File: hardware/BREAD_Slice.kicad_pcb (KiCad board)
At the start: 2 copper layers, 72.6 x 100 mm, 16 parts, among them J1 Conn_01x10_Female, J2 I2C_01x04

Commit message: Initial commit
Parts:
- removed C3, C4: 22uF, Capacitor_SMD:C_1206_3216Metric
- removed D1: WS2812B_5050, SparkFun-LED:WS2812-5050-4PIN
- removed HS1: Heatsink_Pad, SparkFun-Fuse:Thermal Pad
- removed L1: 4.7uH, Inductor_SMD:L_1210_3225Metric
- added J3: Screw_Terminal_01x02, TerminalBlock_TE-Connectivity:TerminalBlock_TE_282834-2_1x02_P2.54mm_Horizontal, F.Cu at (187.8, 83.5)
- added J4: Screw_Terminal_01x02, TerminalBlock_TE-Connectivity:TerminalBlock_TE_282834-2_1x02_P2.54mm_Horizontal, F.Cu at (188.0, 106.7)
- added J5: Screw_Terminal_01x02, TerminalBlock_TE-Connectivity:TerminalBlock_TE_282834-2_1x02_P2.54mm_Horizontal, F.Cu at (188.1, 60.3)
- added U2: ACS723xMATR-10AB, Package_SO:SOIC-16W_7.5x10.3mm_P1.27mm, B.Cu at (175.8, 82.1)
- added U3: ACS723xMATR-10AB, Package_SO:SOIC-16W_7.5x10.3mm_P1.27mm, B.Cu at (175.6, 105.1)
- added U4: ACS723xMATR-10AB, Package_SO:SOIC-16W_7.5x10.3mm_P1.27mm, B.Cu at (175.8, 58.8)
- C1: value 22uF -> 10uF_t; footprint Capacitor_SMD:C_1206_3216Metric -> OCI_UPL_FOOTPRINTS:C_2312
- C2: value 100nF -> 10uF_t; footprint Capacitor_SMD:C_1206_3216Metric -> OCI_UPL_FOOTPRINTS:C_2312
- H1, H4: footprint MountingHole:MountingHole_5mm -> MountingHole:MountingHole_3.2mm_M3_DIN965_Pad
- H2: renamed from H3; footprint MountingHole:MountingHole_5mm -> MountingHole:MountingHole_3.2mm_M3_DIN965_Pad
- H3: renamed from H2; footprint MountingHole:MountingHole_5mm -> MountingHole:MountingHole_3.2mm_M3_DIN965_Pad
- J2: value I2C_01x04 -> Screw_Terminal_01x02; footprint Connector_JST:JST_SH_SM04B-SRSS-TB_1x04-1MP_P1.00mm_Horizontal -> TerminalBlock_TE-Connectivity:TerminalBlock_TE_282834-2_1x02_P2.54mm_Horizontal; moved to F.Cu
- U1: value ~ -> ACS723xMATR-10AB; footprint Package_TO_SOT_SMD:TSOT-23-6 -> Package_SO:SOIC-16W_7.5x10.3mm_P1.27mm
- moved Logo1 76.2 mm to (168.3, 136.0), turned to 0 degrees
- moved U1 47.5 mm to (176.2, 125.4), turned to 180 degrees
- moved J2 38.7 mm to (187.8, 127.0), turned to 90 degrees
- moved C1 37.9 mm to (150.3, 88.4), turned to 90 degrees
- moved C2 27.7 mm to (154.2, 110.8), turned to -90 degrees
- moved A1 7.59 mm to (135.0, 100.0)
- moved J1 3.43 mm to (129.6, 78.8)
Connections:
- A1 pad 1: unconnected-(A1-D1/TX-Pad1) -> Net-(A1-Pad1)
- A1 pad 10: unconnected-(A1-D7-Pad10) -> Net-(A1-Pad10)
- A1 pad 11: unconnected-(A1-D8-Pad11) -> Net-(A1-Pad11)
- A1 pad 12: unconnected-(A1-D9-Pad12) -> Net-(A1-Pad12)
- A1 pad 13: unconnected-(A1-D10-Pad13) -> Net-(A1-Pad13)
- A1 pad 14: unconnected-(A1-D11-Pad14) -> Net-(A1-Pad14)
- A1 pad 15: unconnected-(A1-D12-Pad15) -> Net-(A1-Pad15)
- A1 pad 16: unconnected-(A1-D13-Pad16) -> Net-(A1-Pad16)
- A1 pad 17: unconnected-(A1-3V3-Pad17) -> Net-(A1-Pad17)
- A1 pad 18: unconnected-(A1-AREF-Pad18) -> Net-(A1-Pad18)
- A1 pad 19: unconnected-(A1-A0-Pad19) -> /CURR1
- A1 pad 2: unconnected-(A1-D0/RX-Pad2) -> Net-(A1-Pad2)
- A1 pad 20: unconnected-(A1-A1-Pad20) -> /CURR2
- A1 pad 21: unconnected-(A1-A2-Pad21) -> /CURR3
- A1 pad 22: unconnected-(A1-A3-Pad22) -> /CURR4
- A1 pad 25: unconnected-(A1-A6-Pad25) -> Net-(A1-Pad25)
- A1 pad 26: unconnected-(A1-A7-Pad26) -> Net-(A1-Pad26)
- A1 pad 28: unconnected-(A1-~{RESET}-Pad28) -> Net-(A1-Pad28)
- A1 pad 3: unconnected-(A1-~{RESET}-Pad3) -> Net-(A1-Pad3)
- A1 pad 30: unconnected-(A1-VIN-Pad30) -> +12V
- A1 pad 8: /LED -> Net-(A1-Pad8)
- A1 pad 9: unconnected-(A1-D6-Pad9) -> Net-(A1-Pad9)
- C1 pad 1: GND -> +12V
- C1 pad 2: +12V -> GND
- C2 pad 1: Net-(U1-SW) -> +5V
- C2 pad 2: Net-(U1-BST) -> GND
- J2 pad 1: GND -> Net-(J2-Pad1)
- J2 pad 2: +5V -> Net-(J2-Pad2)
- U1 pad 1: +5V -> Net-(J2-Pad2)
- U1 pad 2: +12V -> Net-(J2-Pad2)
- U1 pad 3: +12V -> Net-(J2-Pad2)
- U1 pad 4: GND -> Net-(J2-Pad2)
- U1 pad 5: Net-(U1-SW) -> Net-(J2-Pad1)
- U1 pad 6: Net-(U1-BST) -> Net-(J2-Pad1)
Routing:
- net +5V: track 108.9 -> 188.6 mm, vias 1 -> 0
- net /CURR4: track 0.00 -> 77.8 mm
- net /CURR3: track 0.00 -> 56.6 mm
- net /LED: track 51.5 -> 0.00 mm
- net /CURR2: track 0.00 -> 36.1 mm
- net /I2C_CLK: track 78.5 -> 46.0 mm, vias 2 -> 0
- net /I2C_DAT: track 76.6 -> 46.4 mm, vias 2 -> 0
- net /CURR1: track 0.00 -> 22.1 mm
- net +12V: track 46.8 -> 58.5 mm
- net GND: track 19.6 -> 30.9 mm, vias 14 -> 0
- net /E_STOP: track 30.1 -> 22.3 mm
- net /INT: track 28.8 -> 22.6 mm
- net /SYNC: track 27.9 -> 22.2 mm
- net Net-(U1-SW): track 5.22 -> 0.00 mm
- net Net-(U1-BST): track 2.64 -> 0.00 mm
- added copper zone on B.Cu, net Net-(J2-Pad1)
- added copper zone on B.Cu, net Net-(J2-Pad2)
- added copper zone on B.Cu, net Net-(J3-Pad1)
- added copper zone on B.Cu, net Net-(J3-Pad2)
- added copper zone on B.Cu, net Net-(J4-Pad1)
- added copper zone on B.Cu, net Net-(J4-Pad2)
- added copper zone on B.Cu, net Net-(J5-Pad1)
- added copper zone on B.Cu, net Net-(J5-Pad2)
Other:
- board size 72.6 x 100 mm -> 70 x 100 mm
- board text added: "10A Current Slice SLC_CR10 R0 2021"
- board text removed: "12V"
- board text removed: "12V->5V Reg"
- board text removed: "5V I2C Connector"
- board text removed: "ARDUINO NANO"
- board text removed: "BREAD Slice Template SLC_TEMP <version> <year>"
- board text removed: "ESTOP"
- board text removed: "GND"
- board text removed: "INT"
- board text removed: "LED"
- board text removed: "SCL"
- board text removed: "SDA"
- board text removed: "SYNC"

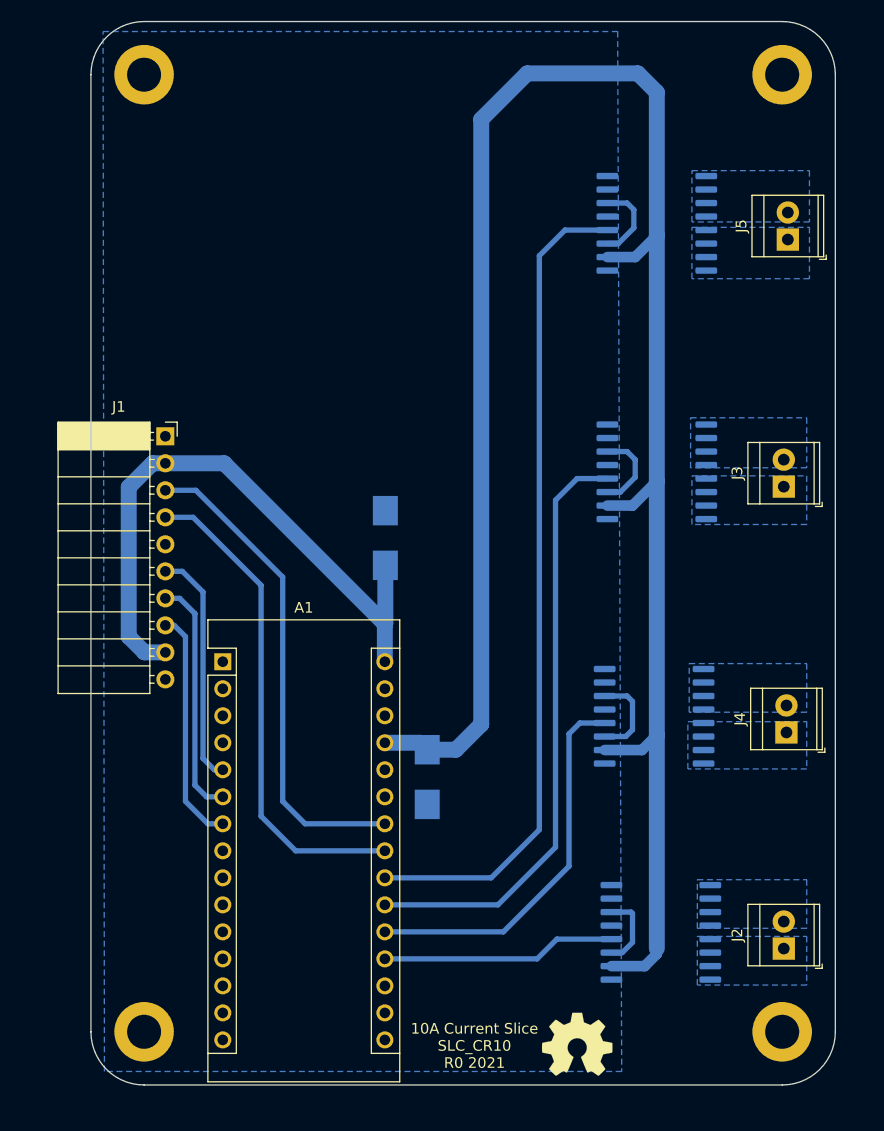
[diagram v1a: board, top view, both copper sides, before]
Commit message: updated to new BREAD format
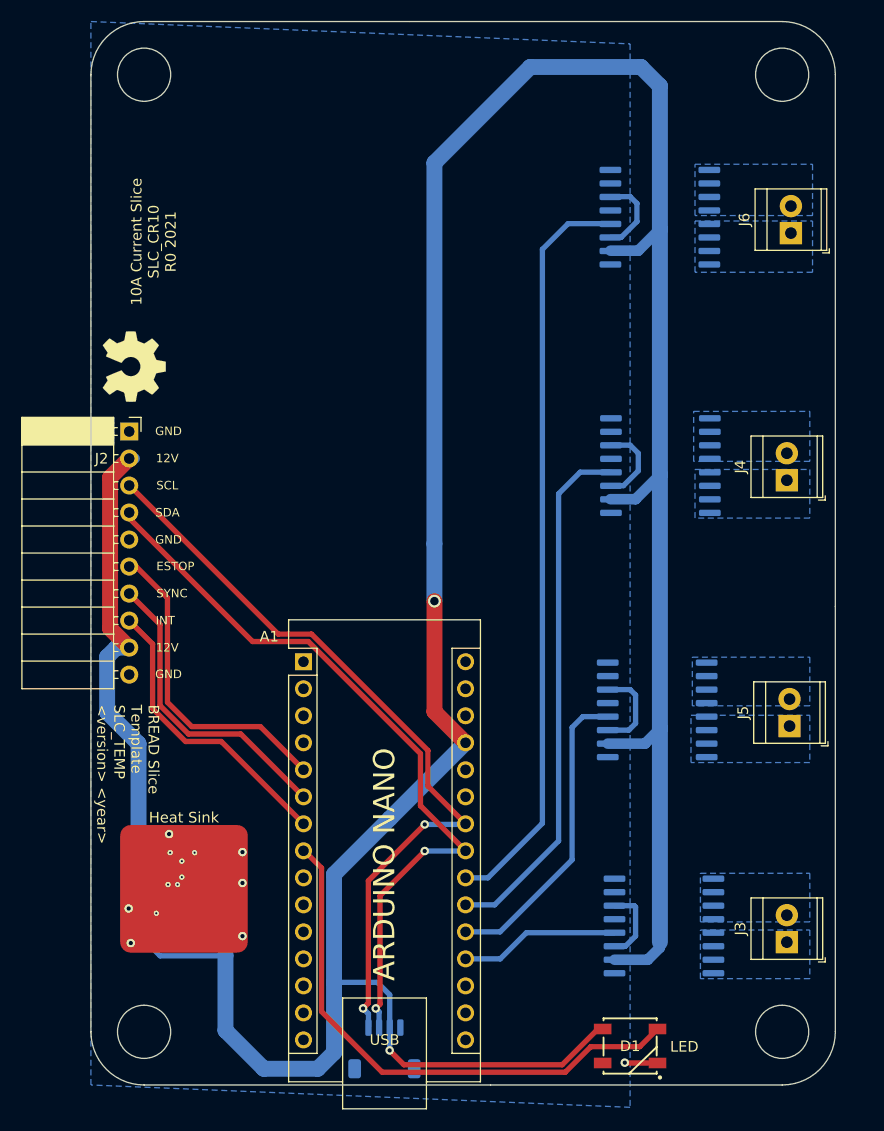
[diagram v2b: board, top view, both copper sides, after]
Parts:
- removed the J2 at (187.8, 127.0)
- added C3: 22uF, Capacitor_SMD:C_1206_3216Metric, B.Cu at (133.8, 119.5)
- added C4: 22uF, Capacitor_SMD:C_1206_3216Metric, B.Cu at (133.8, 116.5)
- added D1: WS2812B_5050, SparkFun-LED:WS2812-5050-4PIN, F.Cu at (173.3, 136.1)
- added HS1: Heatsink_Pad, KML-Custom:Thermal Pad, F.Cu at (131.3, 121.4)
- added J1: I2C_01x04, Connector_JST:JST_SH_SM04B-SRSS-TB_1x04-1MP_P1.00mm_Horizontal, B.Cu at (150.2, 136.4)
- added J6: Screw_Terminal_01x02, TerminalBlock_TE-Connectivity:TerminalBlock_TE_282834-2_1x02_P2.54mm_Horizontal, F.Cu at (188.4, 59.7)
- added L1: 4.7uH, Inductor_SMD:L_1210_3225Metric, B.Cu at (133.8, 122.8)
- added U5: ACS723xMATR-10AB, Package_SO:SOIC-16W_7.5x10.3mm_P1.27mm, B.Cu at (176.1, 58.2)
- C1: value 10uF_t -> 22uF; footprint OCI_UPL_FOOTPRINTS:C_2312 -> Capacitor_SMD:C_1206_3216Metric
- C2: value 10uF_t -> 100nF; footprint OCI_UPL_FOOTPRINTS:C_2312 -> Capacitor_SMD:C_1206_3216Metric
- H1, H4: footprint MountingHole:MountingHole_3.2mm_M3_DIN965_Pad -> MountingHole:MountingHole_5mm
- H2: renamed from H3; footprint MountingHole:MountingHole_3.2mm_M3_DIN965_Pad -> MountingHole:MountingHole_5mm
- H3: renamed from H2; footprint MountingHole:MountingHole_3.2mm_M3_DIN965_Pad -> MountingHole:MountingHole_5mm
- U1: value ACS723xMATR-10AB -> ~; footprint Package_SO:SOIC-16W_7.5x10.3mm_P1.27mm -> Package_TO_SOT_SMD:TSOT-23-6
- moved Logo1 76.2 mm to (126.7, 72.2), turned to -90 degrees
- moved U1 47.5 mm to (128.8, 122.8), turned to 0 degrees
- moved J5 45.8 mm to (188.3, 106.1)
- moved U4 45.8 mm to (175.8, 104.5)
- moved J3 42.8 mm to (188.0, 126.4)
- moved U2 42.7 mm to (176.5, 124.8)
- moved C1 37.9 mm to (128.6, 119.5), turned to 180 degrees
- moved C2 27.7 mm to (131.2, 126.3), turned to 180 degrees
- moved J4 23.7 mm to (188.0, 82.9)
- moved U3 23.6 mm to (176.2, 81.6)
- moved A1 7.59 mm to (142.6, 100.0)
- moved J2 3.43 mm to (126.2, 78.3)
- renumbered J1 to J2
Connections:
- A1 pad 1: Net-(A1-Pad1) -> unconnected-(A1-D1/TX-Pad1)
- A1 pad 10: Net-(A1-Pad10) -> unconnected-(A1-D7-Pad10)
- A1 pad 11: Net-(A1-Pad11) -> unconnected-(A1-D8-Pad11)
- A1 pad 12: Net-(A1-Pad12) -> unconnected-(A1-D9-Pad12)
- A1 pad 13: Net-(A1-Pad13) -> unconnected-(A1-D10-Pad13)
- A1 pad 14: Net-(A1-Pad14) -> unconnected-(A1-D11-Pad14)
- A1 pad 15: Net-(A1-Pad15) -> unconnected-(A1-D12-Pad15)
- A1 pad 16: Net-(A1-Pad16) -> unconnected-(A1-D13-Pad16)
- A1 pad 17: Net-(A1-Pad17) -> unconnected-(A1-3V3-Pad17)
- A1 pad 18: Net-(A1-Pad18) -> unconnected-(A1-AREF-Pad18)
- A1 pad 2: Net-(A1-Pad2) -> unconnected-(A1-D0/RX-Pad2)
- A1 pad 25: Net-(A1-Pad25) -> unconnected-(A1-A6-Pad25)
- A1 pad 26: Net-(A1-Pad26) -> unconnected-(A1-A7-Pad26)
- A1 pad 28: Net-(A1-Pad28) -> unconnected-(A1-~{RESET}-Pad28)
- A1 pad 3: Net-(A1-Pad3) -> unconnected-(A1-~{RESET}-Pad3)
- A1 pad 30: +12V -> unconnected-(A1-VIN-Pad30)
- A1 pad 8: Net-(A1-Pad8) -> /LED
- A1 pad 9: Net-(A1-Pad9) -> unconnected-(A1-D6-Pad9)
- C1 pad 1: +12V -> GND
- C1 pad 2: GND -> +12V
- C2 pad 1: +5V -> Net-(U1-SW)
- C2 pad 2: GND -> Net-(U1-BST)
- U1 pad 1: Net-(J2-Pad2) -> +5V
- U1 pad 2: Net-(J2-Pad2) -> +12V
- U1 pad 3: Net-(J2-Pad2) -> +12V
- U1 pad 4: Net-(J2-Pad2) -> GND
- U1 pad 5: Net-(J2-Pad1) -> Net-(U1-SW)
- U1 pad 6: Net-(J2-Pad1) -> Net-(U1-BST)
- U2 pad 12: /CURR3 -> /CURR1
- U2 pad 16: Net-(U2-Pad16) -> unconnected-(U2-NC-Pad16)
- U2 pad 9: Net-(U2-Pad9) -> unconnected-(U2-NC-Pad9)
- U3 pad 12: /CURR2 -> /CURR3
- U3 pad 16: Net-(U3-Pad16) -> unconnected-(U3-NC-Pad16)
- U3 pad 9: Net-(U3-Pad9) -> unconnected-(U3-NC-Pad9)
- U4 pad 12: /CURR4 -> /CURR2
- U4 pad 16: Net-(U4-Pad16) -> unconnected-(U4-NC-Pad16)
- U4 pad 9: Net-(U4-Pad9) -> unconnected-(U4-NC-Pad9)
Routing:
- net +5V: track 188.6 -> 292.7 mm, vias 0 -> 2
- net /LED: track 0.00 -> 51.5 mm
- net /I2C_CLK: track 46.0 -> 72.3 mm, vias 0 -> 2
- net /I2C_DAT: track 46.4 -> 70.5 mm, vias 0 -> 2
- net GND: track 30.9 -> 50.5 mm, vias 0 -> 14
- net +12V: track 58.5 -> 46.8 mm
- net /E_STOP: track 22.3 -> 30.1 mm
- net /CURR4: track 77.8 -> 70.7 mm
- net /CURR1: track 22.1 -> 15.0 mm
- net /CURR3: track 56.6 -> 49.6 mm
- net /CURR2: track 36.1 -> 29.0 mm
- net /INT: track 22.6 -> 28.8 mm
- net /SYNC: track 22.2 -> 27.9 mm
- net Net-(U1-SW): track 0.00 -> 5.22 mm
- net Net-(U1-BST): track 0.00 -> 2.64 mm
- added copper zone on B.Cu, net Net-(J6-Pin_1)
- added copper zone on B.Cu, net Net-(J6-Pin_2)
- removed copper zone on B.Cu, net Net-(J2-Pad1)
- removed copper zone on B.Cu, net Net-(J2-Pad2)
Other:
- outline, holes or cut-outs redrawn
- board text added: "12V"
- board text added: "12V->5V Reg"
- board text added: "5V I2C Connector"
- board text added: "ARDUINO NANO"
- board text added: "BREAD Slice Template SLC_TEMP <version> <year>"
- board text added: "ESTOP"
- board text added: "GND"
- board text added: "INT"
- board text added: "LED"
- board text added: "SCL"
- board text added: "SDA"
- board text added: "SYNC"

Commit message: updated for CRxx forking
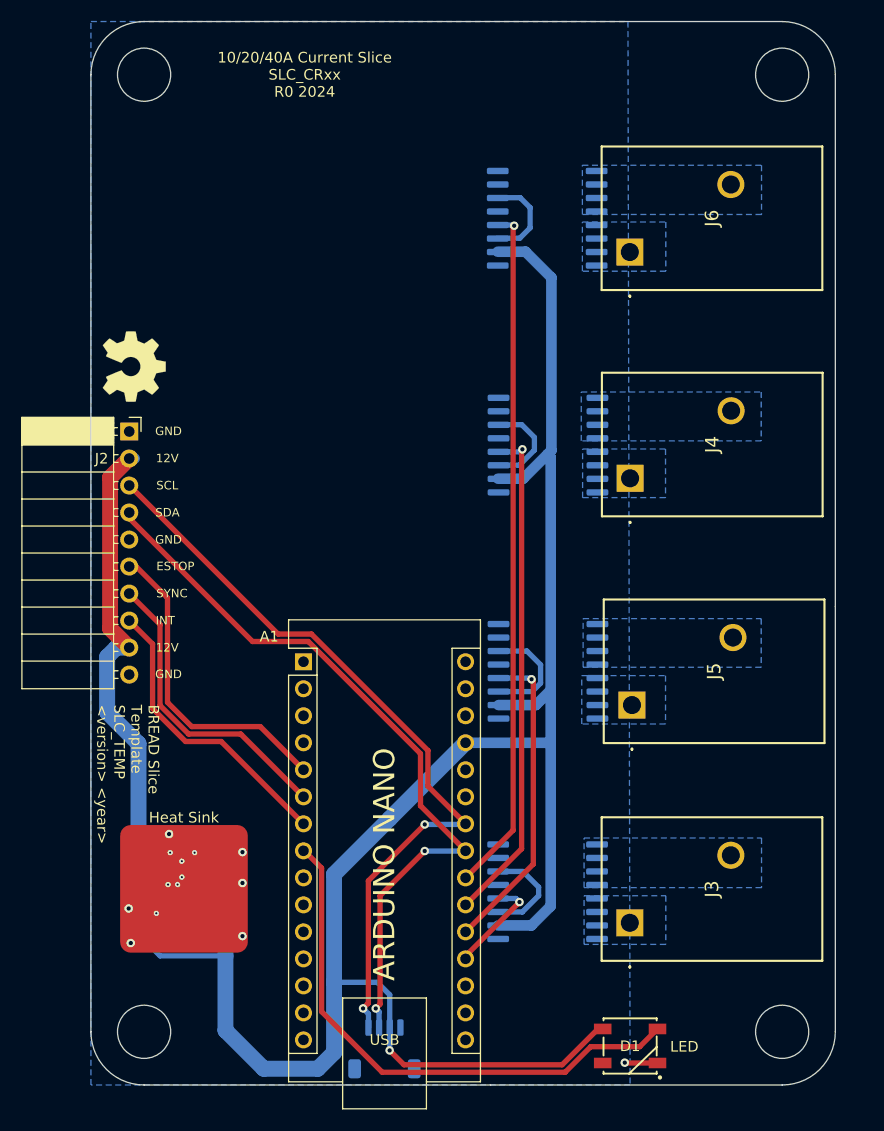
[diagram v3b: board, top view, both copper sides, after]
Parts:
- J3, J4, J5, J6: footprint TerminalBlock_TE-Connectivity:TerminalBlock_TE_282834-2_1x02_P2.54mm_Horizontal -> CRx:Pheonix Conn Term TDPT 4 2-SP-6,35-ZB
- moved J6 15.3 mm to (173.3, 61.5)
- moved J5 15.0 mm to (173.5, 104.1)
- moved J3 14.9 mm to (173.3, 124.5)
- moved J4 14.7 mm to (173.3, 82.8)
- moved U2 11.4 mm to (165.5, 121.6)
- moved U4 10.9 mm to (165.6, 100.9)
- moved U3 10.7 mm to (165.6, 79.6)
- moved U5 10.6 mm to (165.5, 58.3)
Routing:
- net +5V: track 292.7 -> 199.2 mm, vias 2 -> 1
- net GND: track 50.5 -> 57.7 mm
- net /CURR4: track 70.7 -> 64.8 mm, vias 0 -> 1
- net /CURR1: track 15.0 -> 9.59 mm, vias 0 -> 1
- net /CURR3: track 49.6 -> 47.4 mm, vias 0 -> 1
- net /CURR2: track 29.0 -> 29.6 mm, vias 0 -> 1
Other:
- board text added: "10/20/40A Current Slice SLC_CRxx R0 2024"
- board text removed: "10A Current Slice SLC_CR10 R0 2021"
